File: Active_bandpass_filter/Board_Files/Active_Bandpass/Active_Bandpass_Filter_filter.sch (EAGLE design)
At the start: 35 parts, among them IC2 AD8031R, IC3 7805TV, IC5 AD8542R

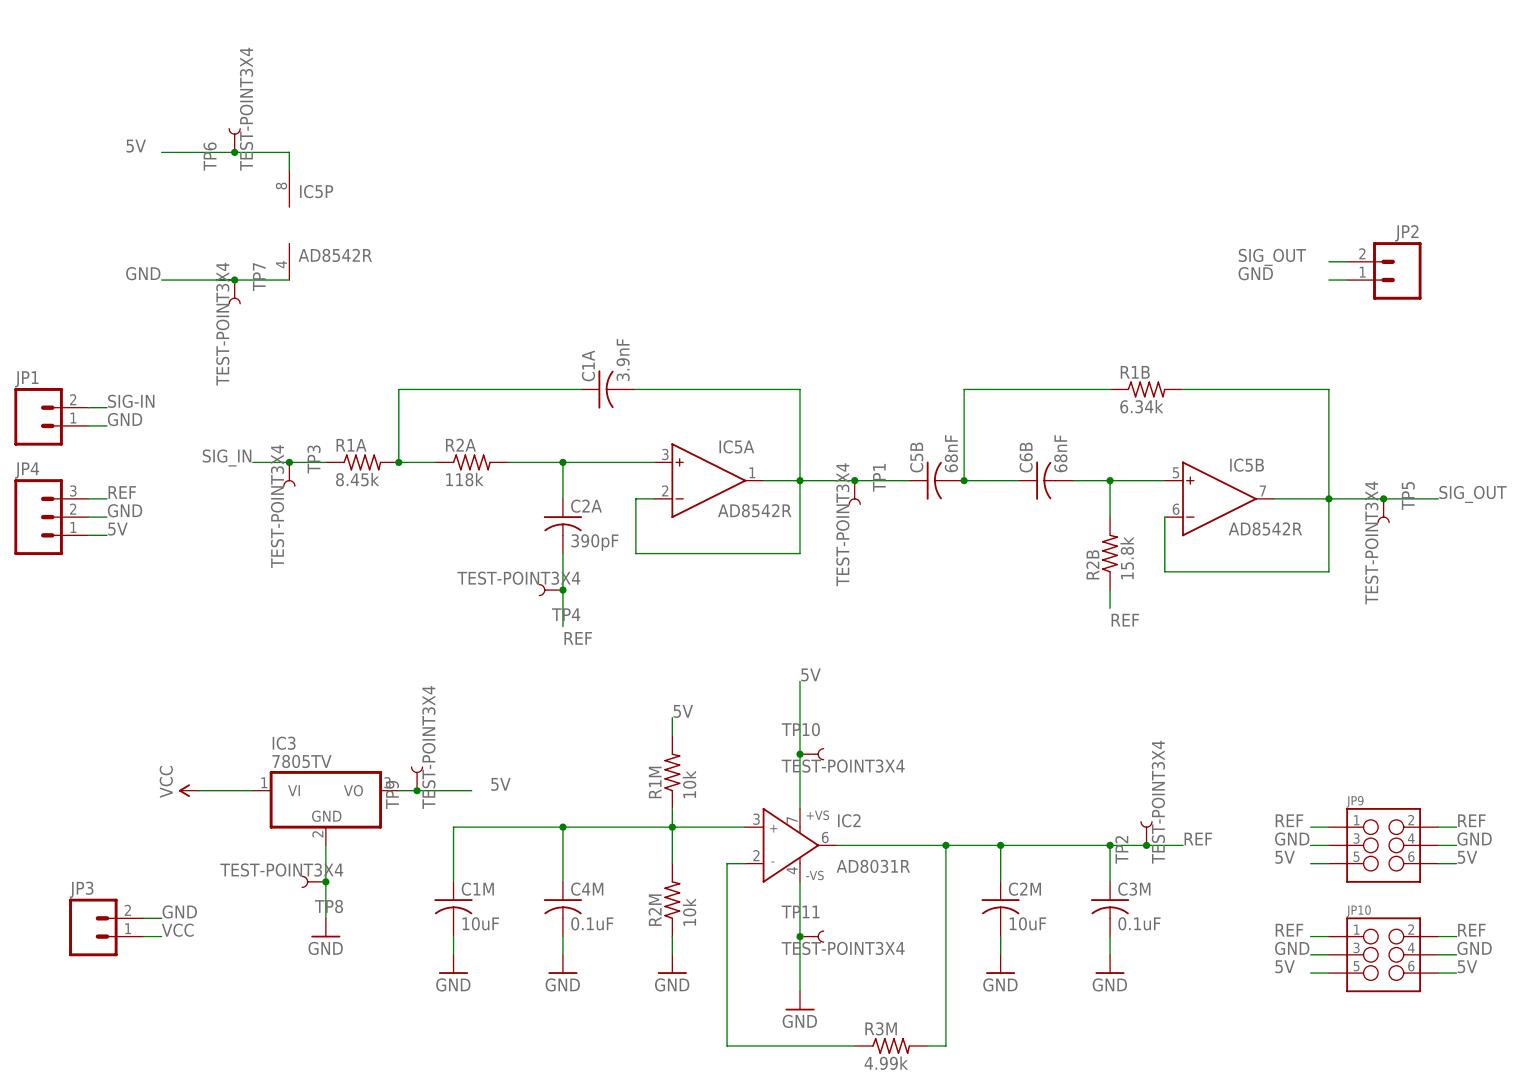
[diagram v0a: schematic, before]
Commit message: split into 2 boards
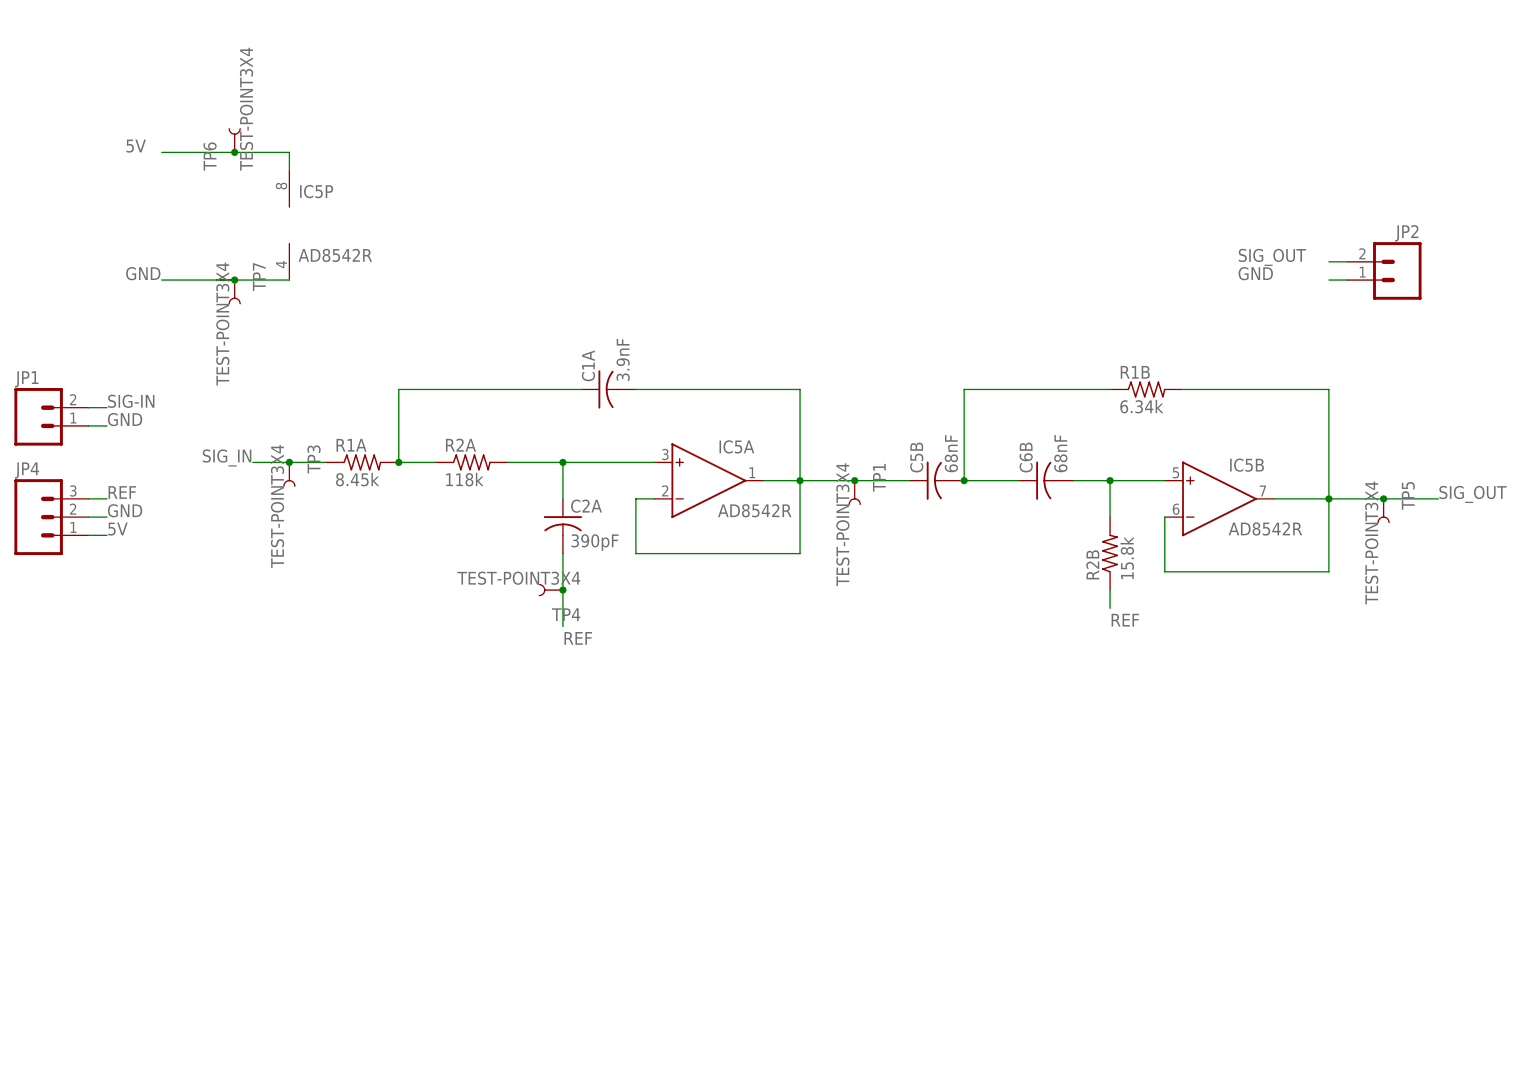
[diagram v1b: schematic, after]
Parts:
- removed C1M, C2M: 10uF, resistor:C-USC1206
- removed C3M, C4M: 0.1uF, resistor:C-USC1206
- removed IC2: AD8031R, analog-devices:AD8031R
- removed IC3: 7805TV, linear:7805TV
- removed JP10, JP9: (no value), SparkFun-Connectors:M03X22X3_SILK_MALE_PTH
- removed JP3: (no value), SparkFun-Connectors:M02LOCK_LONGPADS
- removed R1M, R2M: 10k, resistor:R-US_R1206
- removed R3M: 4.99k, rcl:R-US_R1206
- removed TP10, TP11, TP2, TP8, TP9: TEST-POINT3X4, SparkFun-Passives:TEST-POINT3X4
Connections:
- removed net N$12: IC2.IN-, R3M.1
- removed net N$8: C1M.1, C4M.1, IC2.IN+, R1M.1, R2M.2
- removed net VCC: IC3.VI, JP3.1
- net 5V: no longer IC2.+VS, IC3.VO, JP10.5, JP10.6, JP9.5, JP9.6, R1M.2, TP10.1, TP9.1
- net GND: no longer C1M.2, C2M.2, C3M.2, C4M.2, IC2.-VS, IC3.GND, JP10.3, JP10.4, JP3.2, JP9.3, JP9.4, R2M.1, TP11.1, TP8.1
- net REF: no longer C2M.1, C3M.1, IC2.OUT, JP10.1, JP10.2, JP9.1, JP9.2, R3M.2, TP2.1
